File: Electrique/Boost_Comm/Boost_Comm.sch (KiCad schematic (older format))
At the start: 0 parts

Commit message: Update Template
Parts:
- added R? (x7): R, symbol Device:R
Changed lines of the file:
@@
 Comment4 ""
 $EndDescr
+$Comp
+L Device:R R?
+U 1 1 5E55C861
+P 3150 4800
+F 0 "R?" H 3220 4846 50  0000 L CNN
+F 1 "R" H 3220 4755 50  0000 L CNN
+F 2 "" V 3080 4800 50  0001 C CNN
+F 3 "~" H 3150 4800 50  0001 C CNN
+	1    3150 4800
+	1    0    0    -1
+$EndComp
+$Comp
+L Device:R R?
+U 1 1 5E55CD34
+P 6350 5900
+F 0 "R?" H 6420 5946 50  0000 L CNN
+F 1 "R" H 6420 5855 50  0000 L CNN
+F 2 "" V 6280 5900 50  0001 C CNN
+F 3 "~" H 6350 5900 50  0001 C CNN
+	1    6350 5900
+	-1   0    0    1
+$EndComp
+$Comp
+L Device:R R?
+U 1 1 5E55D086
+P 6150 4750
+F 0 "R?" H 6220 4796 50  0000 L CNN
+F 1 "R" H 6220 4705 50  0000 L CNN
+F 2 "" V 6080 4750 50  0001 C CNN
+F 3 "~" H 6150 4750 50  0001 C CNN
+	1    6150 4750
+	0    -1   -1   0
+$EndComp
+$Comp
+L Device:R R?
+U 1 1 5E55D43D
+P 6150 4050
+F 0 "R?" H 6220 4096 50  0000 L CNN
+F 1 "R" H 6220 4005 50  0000 L CNN
+F 2 "" V 6080 4050 50  0001 C CNN
+F 3 "~" H 6150 4050 50  0001 C CNN
+	1    6150 4050
+	0    -1   -1   0
+$EndComp
+$Comp
+L Device:R R?
+U 1 1 5E55D917
+P 4050 3350
+F 0 "R?" H 4120 3396 50  0000 L CNN
+F 1 "R" H 4120 3305 50  0000 L CNN
+F 2 "" V 3980 3350 50  0001 C CNN
+F 3 "~" H 4050 3350 50  0001 C CNN
+	1    4050 3350
+	0    -1   -1   0
+$EndComp
+$Comp
+L Device:R R?
+U 1 1 5E55DD1F
+P 6800 2250
+F 0 "R?" H 6870 2296 50  0000 L CNN
+F 1 "R" H 6870 2205 50  0000 L CNN
+F 2 "" V 6730 2250 50  0001 C CNN
+F 3 "~" H 6800 2250 50  0001 C CNN
+	1    6800 2250
+	0    -1   -1   0
+$EndComp
+$Comp
+L Device:R R?
+U 1 1 5E55E241
+P 6800 2850
+F 0 "R?" H 6870 2896 50  0000 L CNN
+F 1 "R" H 6870 2805 50  0000 L CNN
+F 2 "" V 6730 2850 50  0001 C CNN
+F 3 "~" H 6800 2850 50  0001 C CNN
+	1    6800 2850
+	0    -1   -1   0
+$EndComp
 $EndSCHEMATC

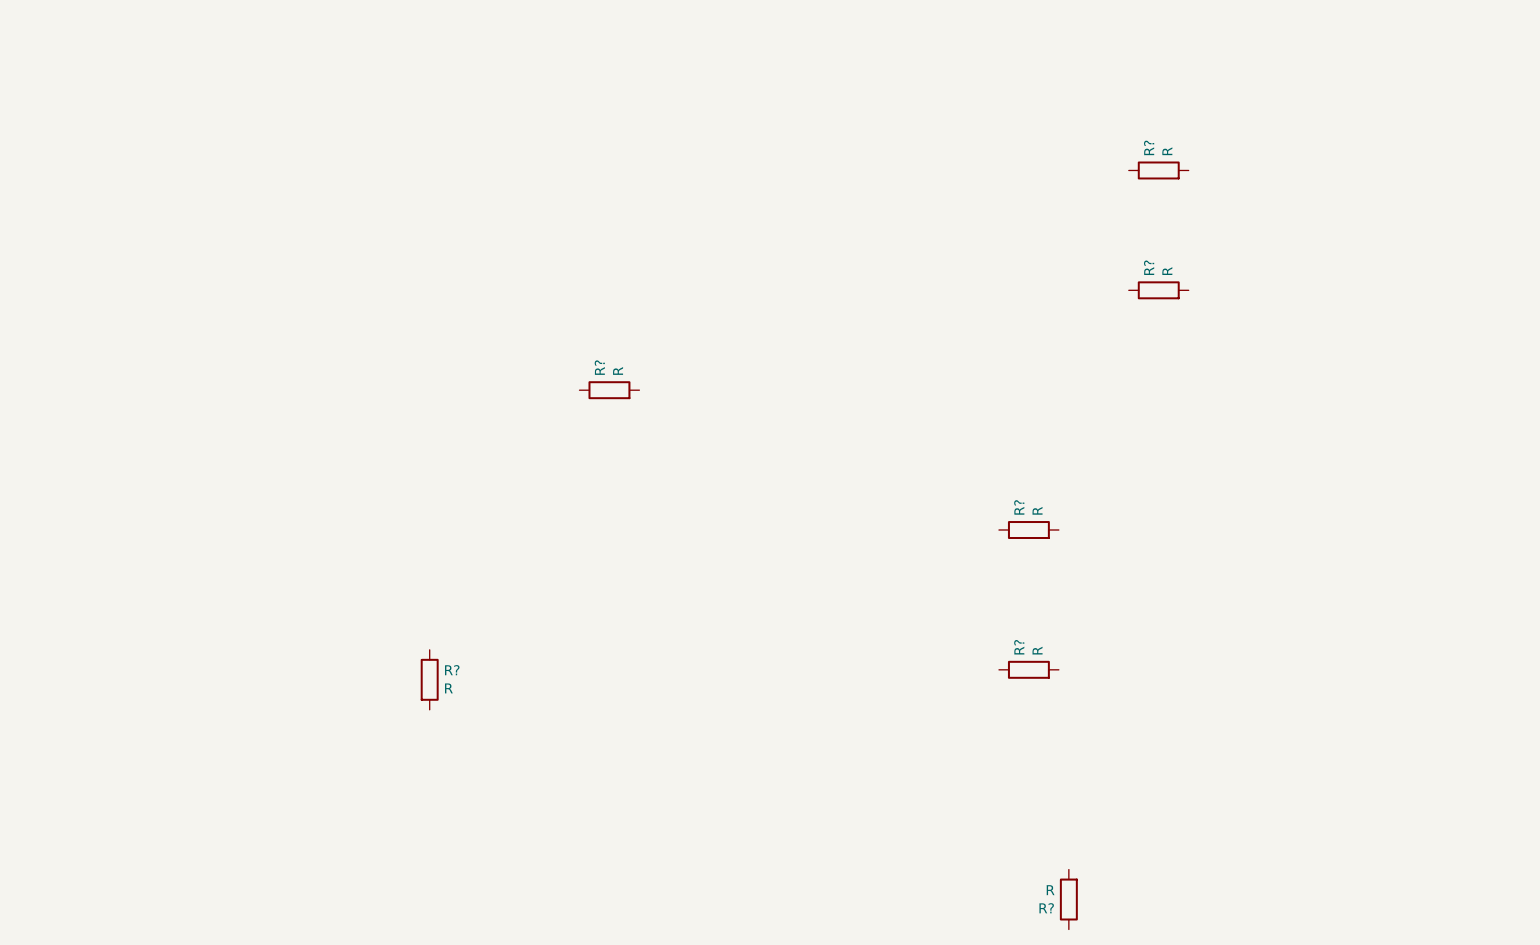
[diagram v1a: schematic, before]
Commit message: Schéma boost Comm fini
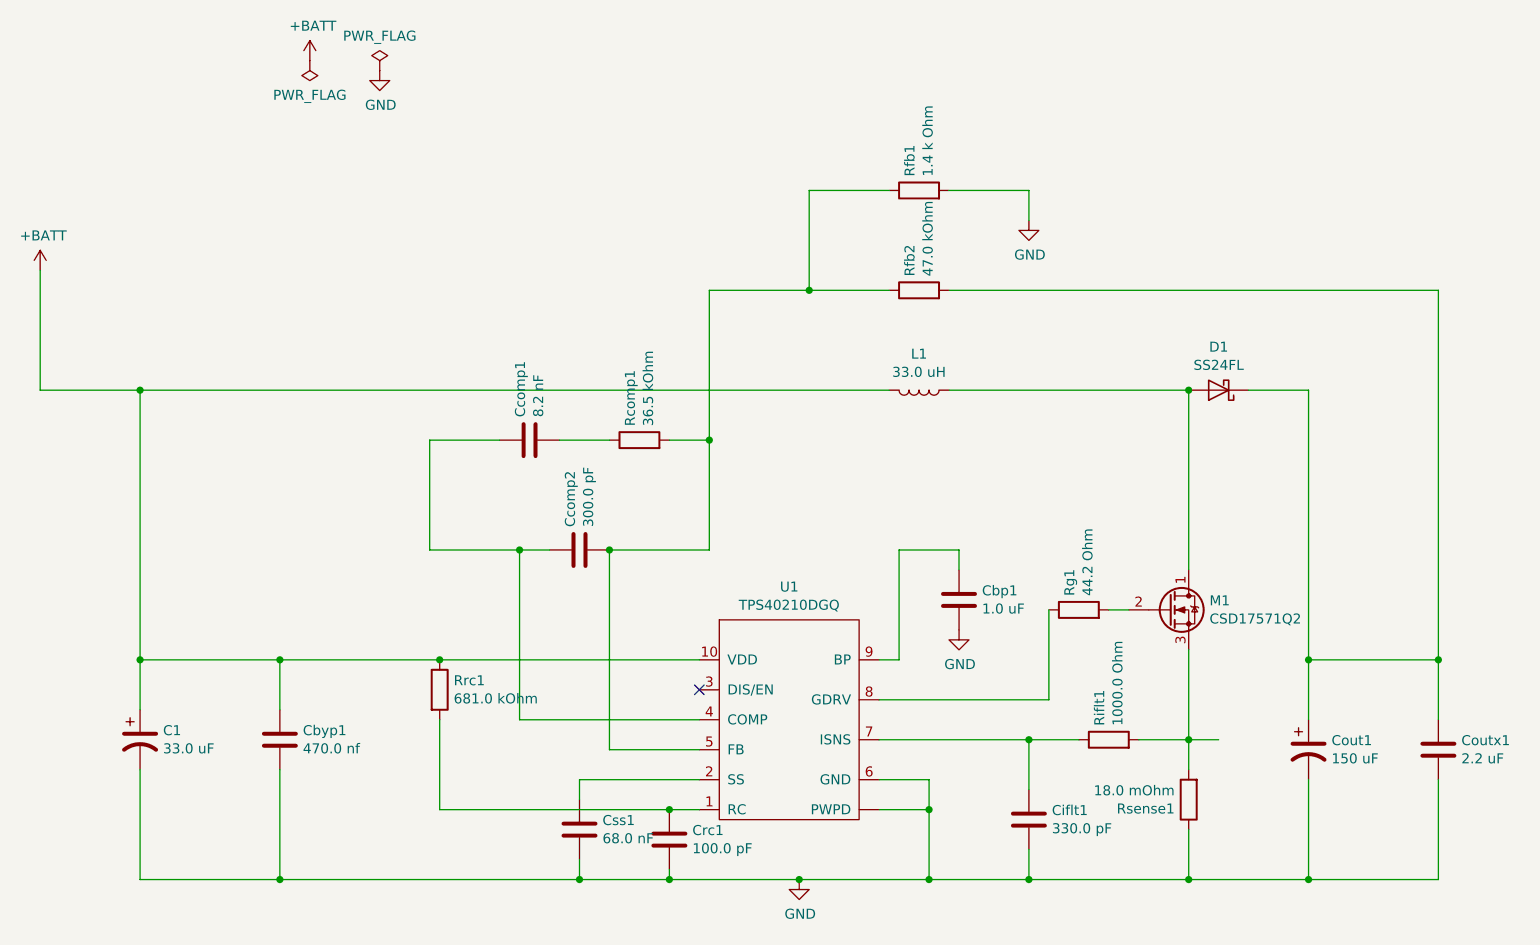
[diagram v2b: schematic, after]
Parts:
- added C1: 33.0 uF, symbol Device:CP1
- added Cbp1: 1.0 uF, symbol Device:C
- added Cbyp1: 470.0 nf, symbol Device:C
- added Ccomp1: 8.2 nF, symbol Device:C
- added Ccomp2: 300.0 pF, symbol Device:C
- added Ciflt1: 330.0 pF, symbol Device:C
- added Cout1: 150 uF, symbol Device:CP1
- added Coutx1: 2.2 uF, symbol Device:C
- added Crc1: 100.0 pF, symbol Device:C
- added Css1: 68.0 nF, symbol Device:C
- added D1: SS24FL, symbol Device:D_Schottky
- added L1: 33.0 uH, symbol Device:L
- added M1: CSD17571Q2, symbol Device:Q_NMOS_DGS
- added U1: TPS40210DGQ, symbol Custom_Boost_Comm:TPS40210DGQ
- Rcomp1: renamed from R?; value R -> 36.5 kOhm; Power_MAX (none) -> 50.0 mW
- Rfb1: renamed from R?; value R -> 1.4 k Ohm; Power_MAX (none) -> 63.0 mW
- Rfb2: renamed from R?; value R -> 47.0 kOhm; Power_MAX (none) -> 100.0 mW
- Rg1: renamed from R?; value R -> 44.2 Ohm; Power_MAX (none) -> 63.0 mW
- Riflt1: renamed from R?; value R -> 1000.0 Ohm; Power_MAX (none) -> 63.0 mW
- Rrc1: renamed from R?; value R -> 681.0 kOhm; Power_max (none) -> 50.0 mW
- Rsense1: renamed from R?; value R -> 18.0 mOhm; Power_MAX (none) -> 1.0 W
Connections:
- net +BATT: now reaches Rrc1.1
- net +BATT: now also C1.1, Cbyp1.1, L1.2, U1.10 (VDD)
- net at Rrc1.2: now also Crc1.1, U1.1 (RC)
- net GND: now reaches Rsense1.1
- net GND: now also Rfb1.2, C1.2, Cbp1.2, Cbyp1.2, Ciflt1.2, Cout1.2, Coutx1.2, Crc1.2, Css1.2, U1.6 (GND), U1.~ (PWPD)
- net at Rsense1.2: now also Riflt1.2, M1.3 (S)
- net at Riflt1.1: now also Ciflt1.1, U1.7 (ISNS)
- net at Rg1.1: now also U1.8 (GDRV)
- net at Rg1.2: now also M1.2 (G)
- net at Rcomp1.1: now also Ccomp1.2
- net at Rcomp1.2: now also Rfb1.1, Rfb2.1, Ccomp2.2, U1.5 (FB)
- net at Rfb2.2: now also Cout1.1, Coutx1.1, D1.1 (K)
- new net: Ccomp1.1, Ccomp2.1, U1.4 (COMP)
- new net: Css1.1, U1.2 (SS)
- new net: Cbp1.1, U1.9 (BP)
- new net: D1.2 (A), L1.1, M1.1 (D)
- no-connect marks 0 -> 1
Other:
- moved on the sheet: Rcomp1, Rfb1, Rfb2, Rg1, Riflt1, Rrc1, Rsense1

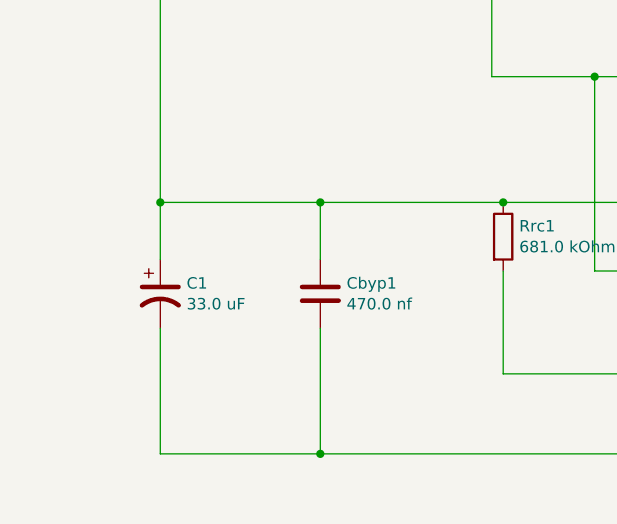
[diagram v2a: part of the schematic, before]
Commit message: Association footprint-composante partielle
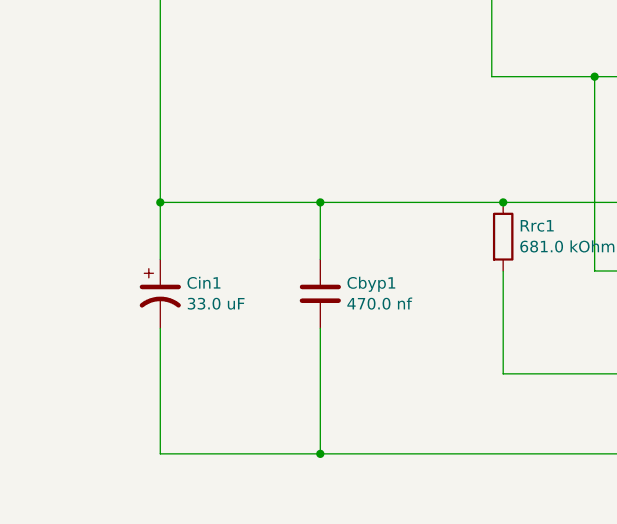
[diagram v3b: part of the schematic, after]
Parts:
- Cbp1, Cbyp1, Ccomp1, Ciflt1, Crc1: footprint (none) -> Capacitor_SMD:C_0805_2012Metric_Pad1.15x1.40mm_HandSolder
- Ccomp2: footprint (none) -> Capacitor_SMD:C_0603_1608Metric_Pad1.05x0.95mm_HandSolder
- Css1: footprint (none) -> Capacitor_SMD:C_0402_1005Metric
- D1: footprint (none) -> Diode_SMD:D_SOD-123F
- Rcomp1, Rrc1: footprint (none) -> Resistor_SMD:R_0201_0603Metric
- Rfb1, Rg1, Riflt1: footprint (none) -> Resistor_SMD:R_0402_1005Metric
- Rfb2: footprint (none) -> Resistor_SMD:R_0603_1608Metric_Pad1.05x0.95mm_HandSolder
- Rsense1: footprint (none) -> Resistor_SMD:R_0612_1632Metric_Pad1.18x3.40mm_HandSolder
- U1: footprint (none) -> Boost_Comm:TSSOP-10_3x3mm_P0.5mm_ThermalPad
- renumbered C1 to Cin1

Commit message: Ajout pieces manquantes Boost
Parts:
- Cbp1, Cbyp1, Ccomp1, Ciflt1: footprint Capacitor_SMD:C_0805_2012Metric_Pad1.15x1.40mm_HandSolder -> Capacitor_SMD:C_0805_2012Metric
- Ccomp2: footprint Capacitor_SMD:C_0603_1608Metric_Pad1.05x0.95mm_HandSolder -> Capacitor_SMD:C_0805_2012Metric
- Cin1: footprint (none) -> Boost_Comm:CAP_EEE-FT1H470AP
- Cout1: footprint (none) -> Boost_Comm:CAP_EEHZA1V151P
- Coutx1: footprint (none) -> Capacitor_SMD:C_1206_3216Metric
- Crc1: footprint Capacitor_SMD:C_0805_2012Metric_Pad1.15x1.40mm_HandSolder -> Capacitor_SMD:C_1206_3216Metric
- L1: footprint (none) -> Inductor_SMD:L_Wuerth_HCI-1365
- M1: footprint (none) -> Boost_Comm:CSD17571Q2
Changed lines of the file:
@@
 F 0 "Ccomp1" H 3765 3646 50  0000 L CNN
 F 1 "8.2 nF" H 3765 3555 50  0000 L CNN
-F 2 "Capacitor_SMD:C_0805_2012Metric_Pad1.15x1.40mm_HandSolder" H 3688 3450 50  0001 C CNN
+F 2 "Capacitor_SMD:C_0805_2012Metric" H 3688 3450 50  0001 C CNN
 F 3 "~" H 3650 3600 50  0001 C CNN
 	1    3650 3600
@@
 F 0 "Cbyp1" H 2515 5146 50  0000 L CNN
 F 1 "470.0 nf" H 2515 5055 50  0000 L CNN
-F 2 "Capacitor_SMD:C_0805_2012Metric_Pad1.15x1.40mm_HandSolder" H 2438 4950 50  0001 C CNN
+F 2 "Capacitor_SMD:C_0805_2012Metric" H 2438 4950 50  0001 C CNN
 F 3 "~" H 2400 5100 50  0001 C CNN
 	1    2400 5100
@@
 F 0 "Cbp1" H 5915 4446 50  0000 L CNN
 F 1 "1.0 uF" H 5915 4355 50  0000 L CNN
-F 2 "Capacitor_SMD:C_0805_2012Metric_Pad1.15x1.40mm_HandSolder" H 5838 4250 50  0001 C CNN
+F 2 "Capacitor_SMD:C_0805_2012Metric" H 5838 4250 50  0001 C CNN
 F 3 "~" H 5800 4400 50  0001 C CNN
 	1    5800 4400
@@
 F 0 "Crc1" H 4465 5646 50  0000 L CNN
 F 1 "100.0 pF" H 4465 5555 50  0000 L CNN
-F 2 "Capacitor_SMD:C_0805_2012Metric_Pad1.15x1.40mm_HandSolder" H 4388 5450 50  0001 C CNN
+F 2 "Capacitor_SMD:C_1206_3216Metric" H 4388 5450 50  0001 C CNN
 F 3 "~" H 4350 5600 50  0001 C CNN
 	1    4350 5600
@@
 F 0 "Ciflt1" H 6265 5546 50  0000 L CNN
 F 1 "330.0 pF" H 6265 5455 50  0000 L CNN
-F 2 "Capacitor_SMD:C_0805_2012Metric_Pad1.15x1.40mm_HandSolder" H 6188 5350 50  0001 C CNN
+F 2 "Capacitor_SMD:C_0805_2012Metric" H 6188 5350 50  0001 C CNN
 F 3 "~" H 6150 5500 50  0001 C CNN
 	1    6150 5500
@@
 F 0 "Ccomp2" H 4015 4196 50  0000 L CNN
 F 1 "300.0 pF" H 4015 4105 50  0000 L CNN
-F 2 "Capacitor_SMD:C_0603_1608Metric_Pad1.05x0.95mm_HandSolder" H 3938 4000 50  0001 C CNN
+F 2 "Capacitor_SMD:C_0805_2012Metric" H 3938 4000 50  0001 C CNN
 F 3 "~" H 3900 4150 50  0001 C CNN
 	1    3900 4150
@@
 F 0 "Cin1" H 1815 5146 50  0000 L CNN
 F 1 "33.0 uF" H 1815 5055 50  0000 L CNN
-F 2 "" H 1700 5100 50  0001 C CNN
+F 2 "Boost_Comm:CAP_EEE-FT1H470AP" H 1700 5100 50  0001 C CNN
 F 3 "~" H 1700 5100 50  0001 C CNN
 	1    1700 5100
@@
 F 0 "Cout1" H 7665 5196 50  0000 L CNN
 F 1 "150 uF" H 7665 5105 50  0000 L CNN
-F 2 "" H 7550 5150 50  0001 C CNN
+F 2 "Boost_Comm:CAP_EEHZA1V151P" H 7550 5150 50  0001 C CNN
 F 3 "~" H 7550 5150 50  0001 C CNN
 	1    7550 5150
@@
 F 0 "M1" H 7054 4496 50  0000 L CNN
 F 1 "CSD17571Q2" H 7054 4405 50  0000 L CNN
-F 2 "" H 7050 4550 50  0001 C CNN
+F 2 "Boost_Comm:CSD17571Q2" H 7050 4550 50  0001 C CNN
 F 3 "~" H 6850 4450 50  0001 C CNN
 	1    6850 4450
@@
 F 0 "Coutx1" H 8315 5196 50  0000 L CNN
 F 1 "2.2 uF" H 8315 5105 50  0000 L CNN
-F 2 "" H 8238 5000 50  0001 C CNN
+F 2 "Capacitor_SMD:C_1206_3216Metric" H 8238 5000 50  0001 C CNN
 F 3 "~" H 8200 5150 50  0001 C CNN
 	1    8200 5150
@@
 F 0 "L1" V 5419 3350 50  0000 C CNN
 F 1 "33.0 uH" V 5510 3350 50  0000 C CNN
-F 2 "" H 5600 3350 50  0001 C CNN
+F 2 "Inductor_SMD:L_Wuerth_HCI-1365" H 5600 3350 50  0001 C CNN
 F 3 "~" H 5600 3350 50  0001 C CNN
 	1    5600 3350

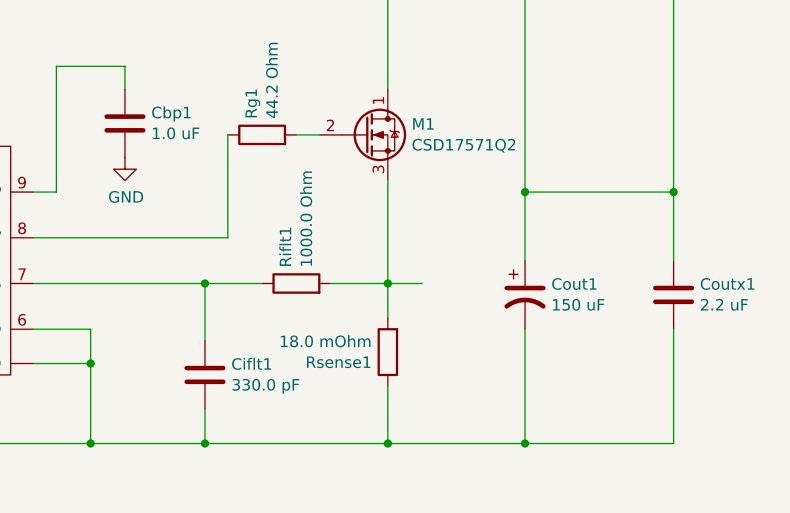
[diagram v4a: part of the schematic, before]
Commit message: Placement initiale des pièces sur pcb
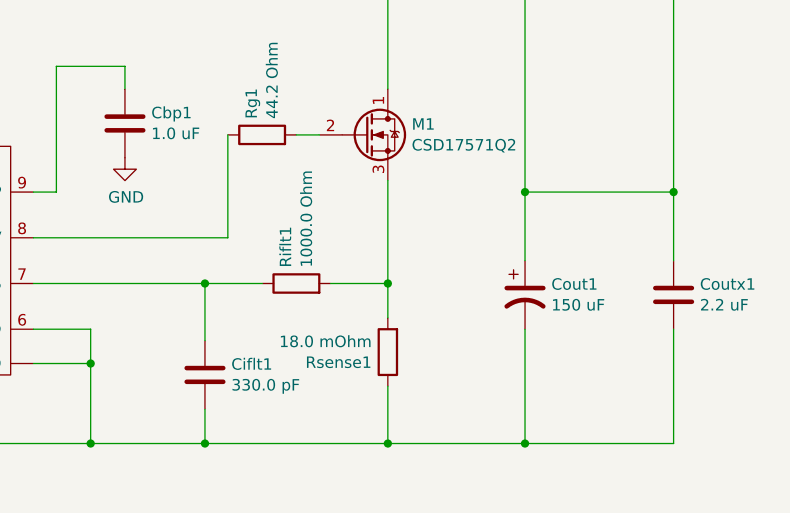
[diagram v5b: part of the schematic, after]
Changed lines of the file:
@@
 	5050 2850 5050 2350
 Connection ~ 6950 5100
-Wire Wire Line
-	6950 5100 7100 5100
 Connection ~ 6950 5800
 Wire Wire Line
